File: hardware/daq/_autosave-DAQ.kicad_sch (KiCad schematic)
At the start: 179 parts, among them J1 ICD15S13E4GX00LF, J2 ICD15S13E4GX00LF, J4 ICD15S13E4GX00LF, J5 ICD15S13E4GX00LF, P1 0022272021, U1 ADS124S08IRHBT, U11 SN74AHCT125RGYR, U2 ADS124S08IRHBT, U3 LT6654BMPS6-5-TRMPBF, U4 LM1086IS-5.0_NOPB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

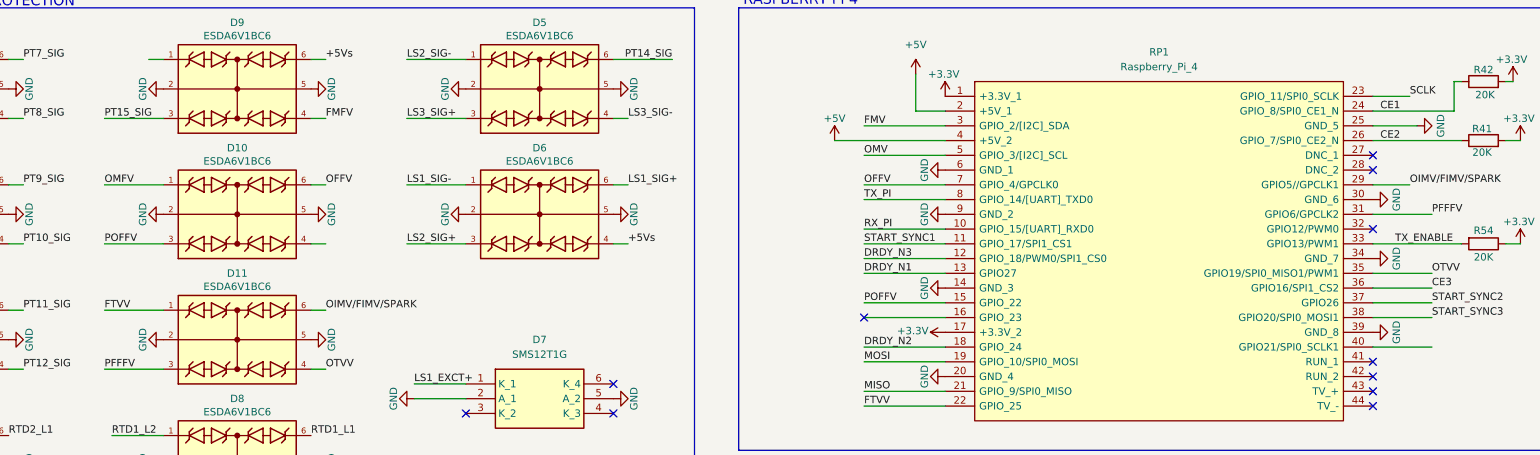
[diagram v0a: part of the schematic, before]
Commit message: properly dimensioned edge cuts and mounting holes
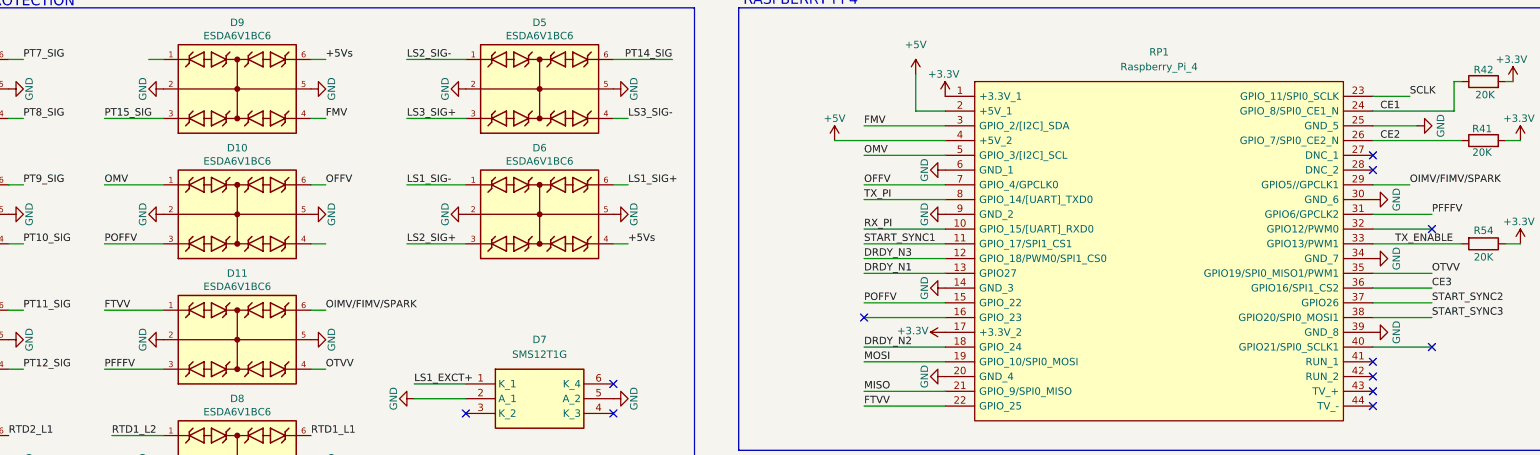
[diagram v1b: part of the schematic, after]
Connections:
- net FMFV is gone; now on net FMV: D9.4
- net OMFV is gone; now on net OMV: D10.1
- no-connect marks 29 -> 30
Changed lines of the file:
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@@
 	)
 	(no_connect
-		(at 530.86 72.39)
+		(at 541.02 72.39)
 	)
 	(no_connect
@@
 	)
 	(no_connect
+		(at 541.02 92.71)
+	)
+	(no_connect
 		(at 523.24 182.88)
 	)
@@
 	(wire
 		(pts
+			(xy 541.02 72.39) (xy 530.86 72.39)
+		)
+		(stroke
+			(width 0)
+			(type default)
+		)
+	)
+	(wire
+		(pts
 			(xy 543.56 276.86) (xy 543.56 275.59)
 		)
@@
 		)
 	)
-	(label "OMFV"
+	(label "OMV"
 		(at 312.42 64.77 0)
 		(effects
@@
 		)
 	)
-	(label "FMFV"
+	(label "FMV"
 		(at 350.52 53.34 0)
 		(effects
